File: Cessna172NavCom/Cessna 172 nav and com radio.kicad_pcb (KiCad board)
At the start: 2 copper layers, 180 x 98 mm, 95 parts, among them J1 EN11-HSM1BF20, J2 USB_B_Micro, J3 EN11-HSM1BF20, J4 EN11-HSM1BF20, J5 EN11-HSM1BF20, J6 EN11-HSM1BF20, J7 EN11-HSM1BF20, J8 Conn_02x20_Odd_Even, SW1 SW_Push, SW2 SW_Push, SW3 SW_Push, SW4 SW_Push, SW5 SW_Push, SW6 SW_Push, U1 MAX7219 COM standby, U10 3651A, U11 MAX7219 COM standby, U12 3651A, U13 MAX7219 COM standby, U14 3651A, U15 MAX7219 COM standby, U16 3651A, U2 3651A, U3 MAX7219 COM standby, U4 3651A, U5 MAX7219 COM standby, U6 3651A, U7 MAX7219 COM standby, U8 3651A, U9 MAX7219 COM standby

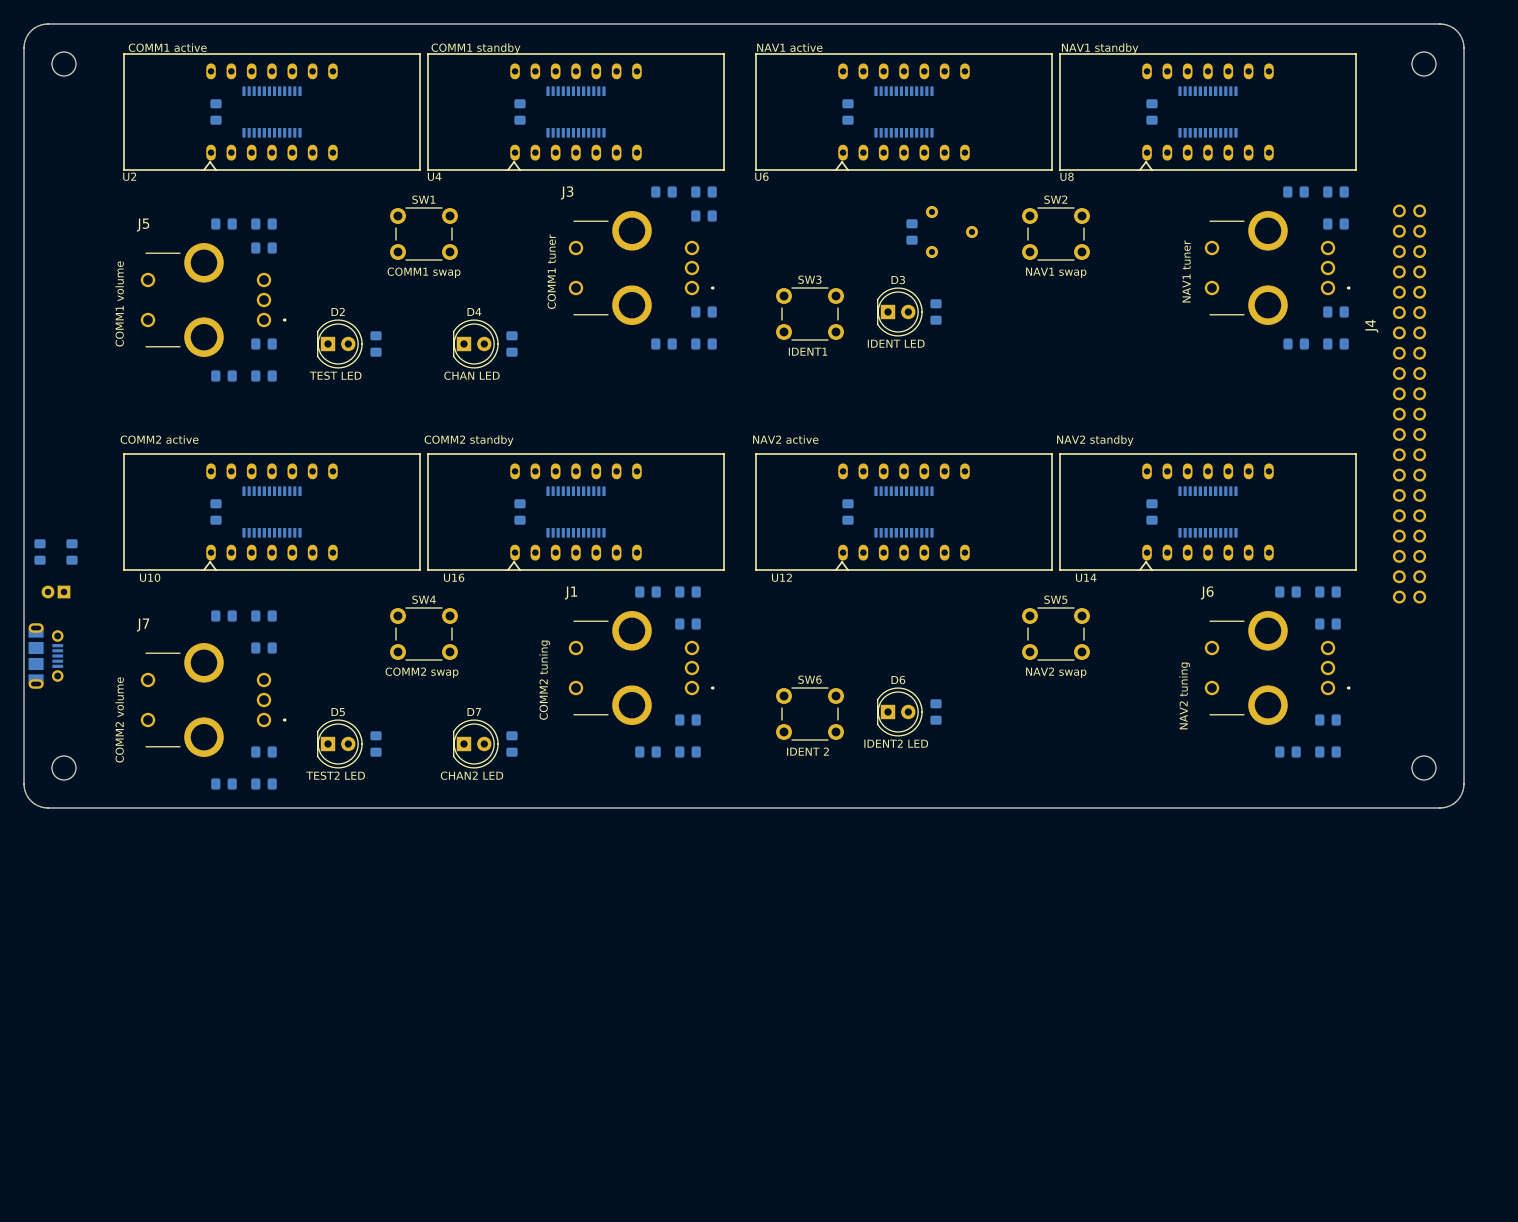
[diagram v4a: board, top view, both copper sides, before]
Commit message: Position changes for routing
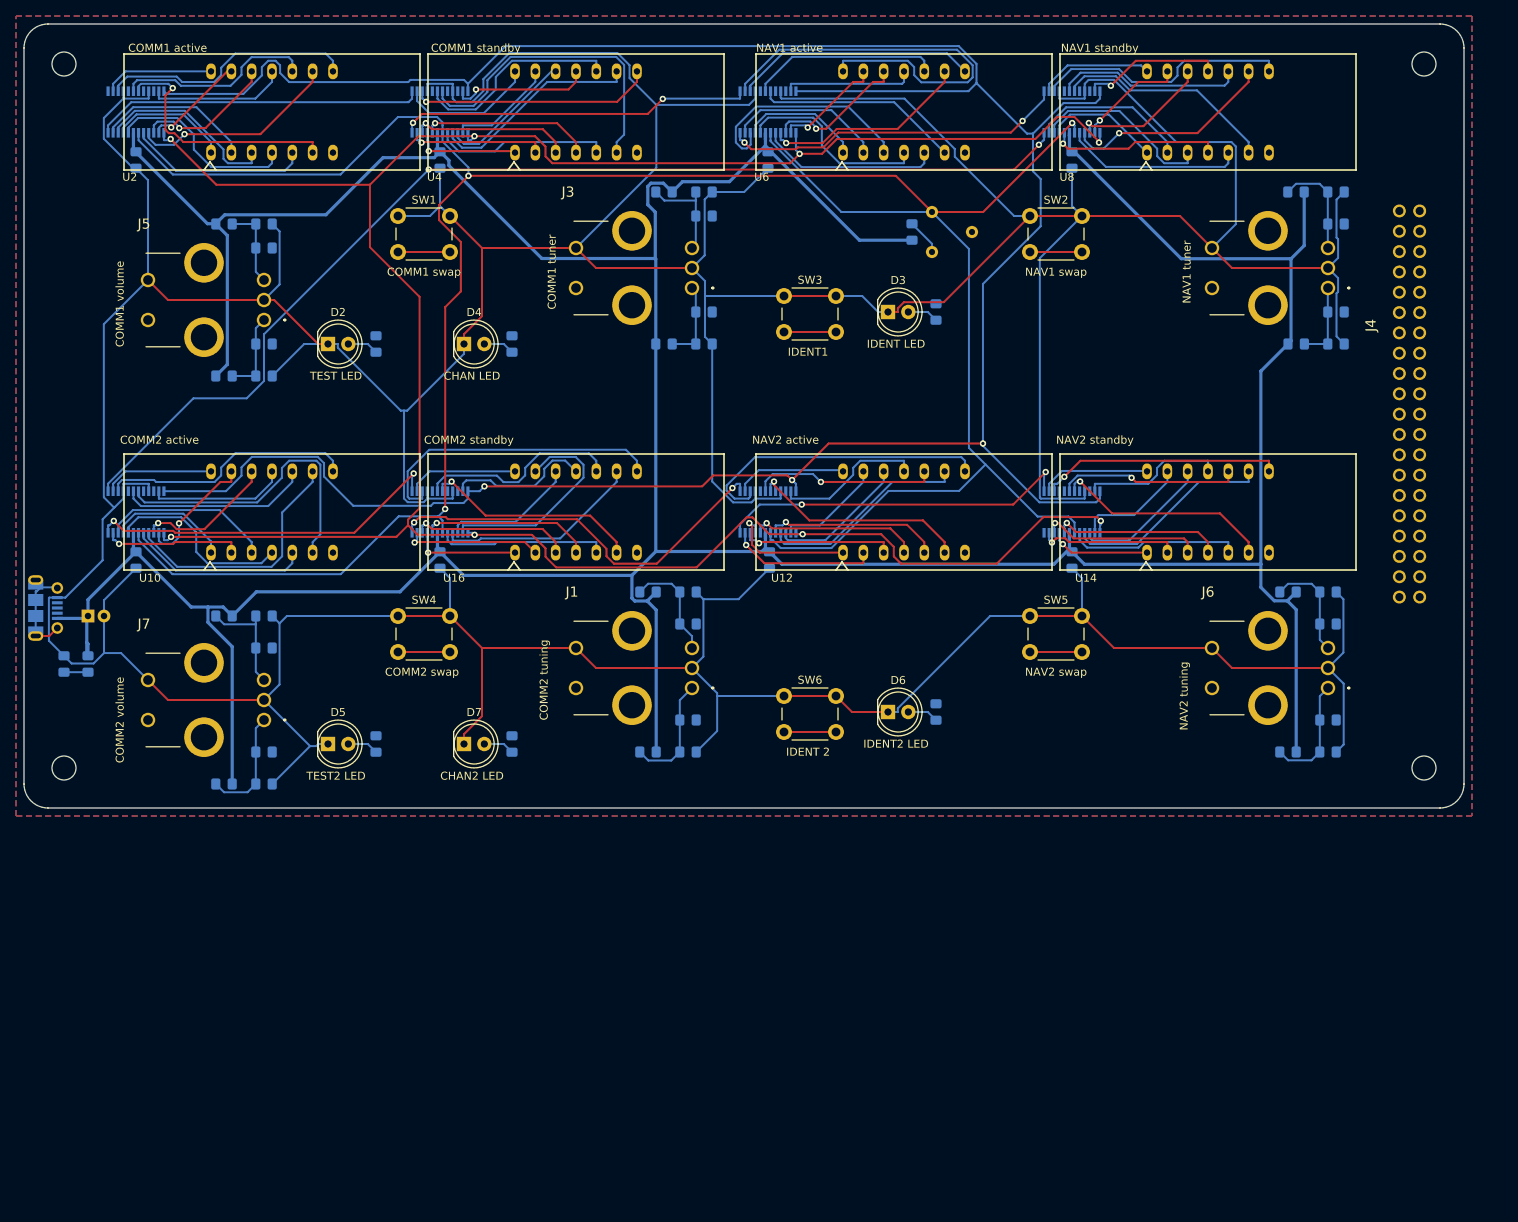
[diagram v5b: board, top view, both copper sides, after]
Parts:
- moved U1 17.0 mm to (44.0, 41.0)
- moved U11 17.0 mm to (123.0, 91.0)
- moved U13 17.0 mm to (161.0, 91.0)
- moved U15 17.0 mm to (82.0, 91.0)
- moved U3 17.0 mm to (82.0, 41.0)
- moved U5 17.0 mm to (123.0, 41.0)
- moved U7 17.0 mm to (161.0, 41.0)
- moved U9 17.0 mm to (44.0, 91.0)
- moved D1 14.3 mm to (35.0, 110.0), turned to 270 degrees
- moved R2 14.1 mm to (38.0, 110.0)
- moved C12 11.7 mm to (44.0, 97.0)
- moved C13 11.7 mm to (82.0, 97.0)
- moved C15 11.7 mm to (161.0, 97.0)
- moved C2 11.7 mm to (44.0, 47.0), turned to 270 degrees
- moved C3 11.7 mm to (82.0, 47.0), turned to 270 degrees
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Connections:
- U10 pad 7: (no net) -> Net-(U10-Pad7)
- U12 pad 7: (no net) -> Net-(U12-Pad7)
- U14 pad 7: (no net) -> Net-(U14-Pad7)
- U16 pad 7: (no net) -> Net-(U16-Pad7)
- U2 pad 7: (no net) -> Net-(U2-Pad7)
- U4 pad 7: (no net) -> Net-(U4-Pad7)
- U6 pad 7: (no net) -> Net-(U6-Pad7)
- U8 pad 7: (no net) -> Net-(U8-Pad7)
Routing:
- net GND: track 0.00 -> 904.7 mm
- net +5V: track 0.00 -> 539.0 mm
- net ISET: track 0.00 -> 334.3 mm, vias 0 -> 3
- net LOAD: track 0.00 -> 331.2 mm, vias 0 -> 3
- net CLK: track 0.00 -> 313.8 mm, vias 0 -> 8
- net /sheet5F68A9C2/DIN: track 0.00 -> 140.1 mm, vias 0 -> 2
- net /sheet5F613960/DIG_0: track 0.00 -> 53.0 mm
- net /sheet5F68A9C3/DIN: track 0.00 -> 50.4 mm, vias 0 -> 2
- net /sheet5F68A9C5/DIN: track 0.00 -> 45.3 mm, vias 0 -> 2
- net /sheet5F68A9C4/DIN: track 0.00 -> 44.5 mm, vias 0 -> 2
- net /sheet5F613960/DIN: track 0.00 -> 44.4 mm, vias 0 -> 2
- net /sheet5F613961/DIN: track 0.00 -> 43.0 mm, vias 0 -> 2
- net /sheet5F611637/DIN: track 0.00 -> 41.2 mm
- net /sheet5F611637/DIG_3: track 0.00 -> 39.2 mm
- net /sheet5F68A9C2/DIG_3: track 0.00 -> 38.2 mm
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- added copper zone on B.Cu, net GND
- added copper zone on F.Cu, net GND
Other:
- rule trace_min: 0.2 -> 0.15
- rule via_min_size: 0.4 -> 0.3

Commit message: Move things around to try and help router
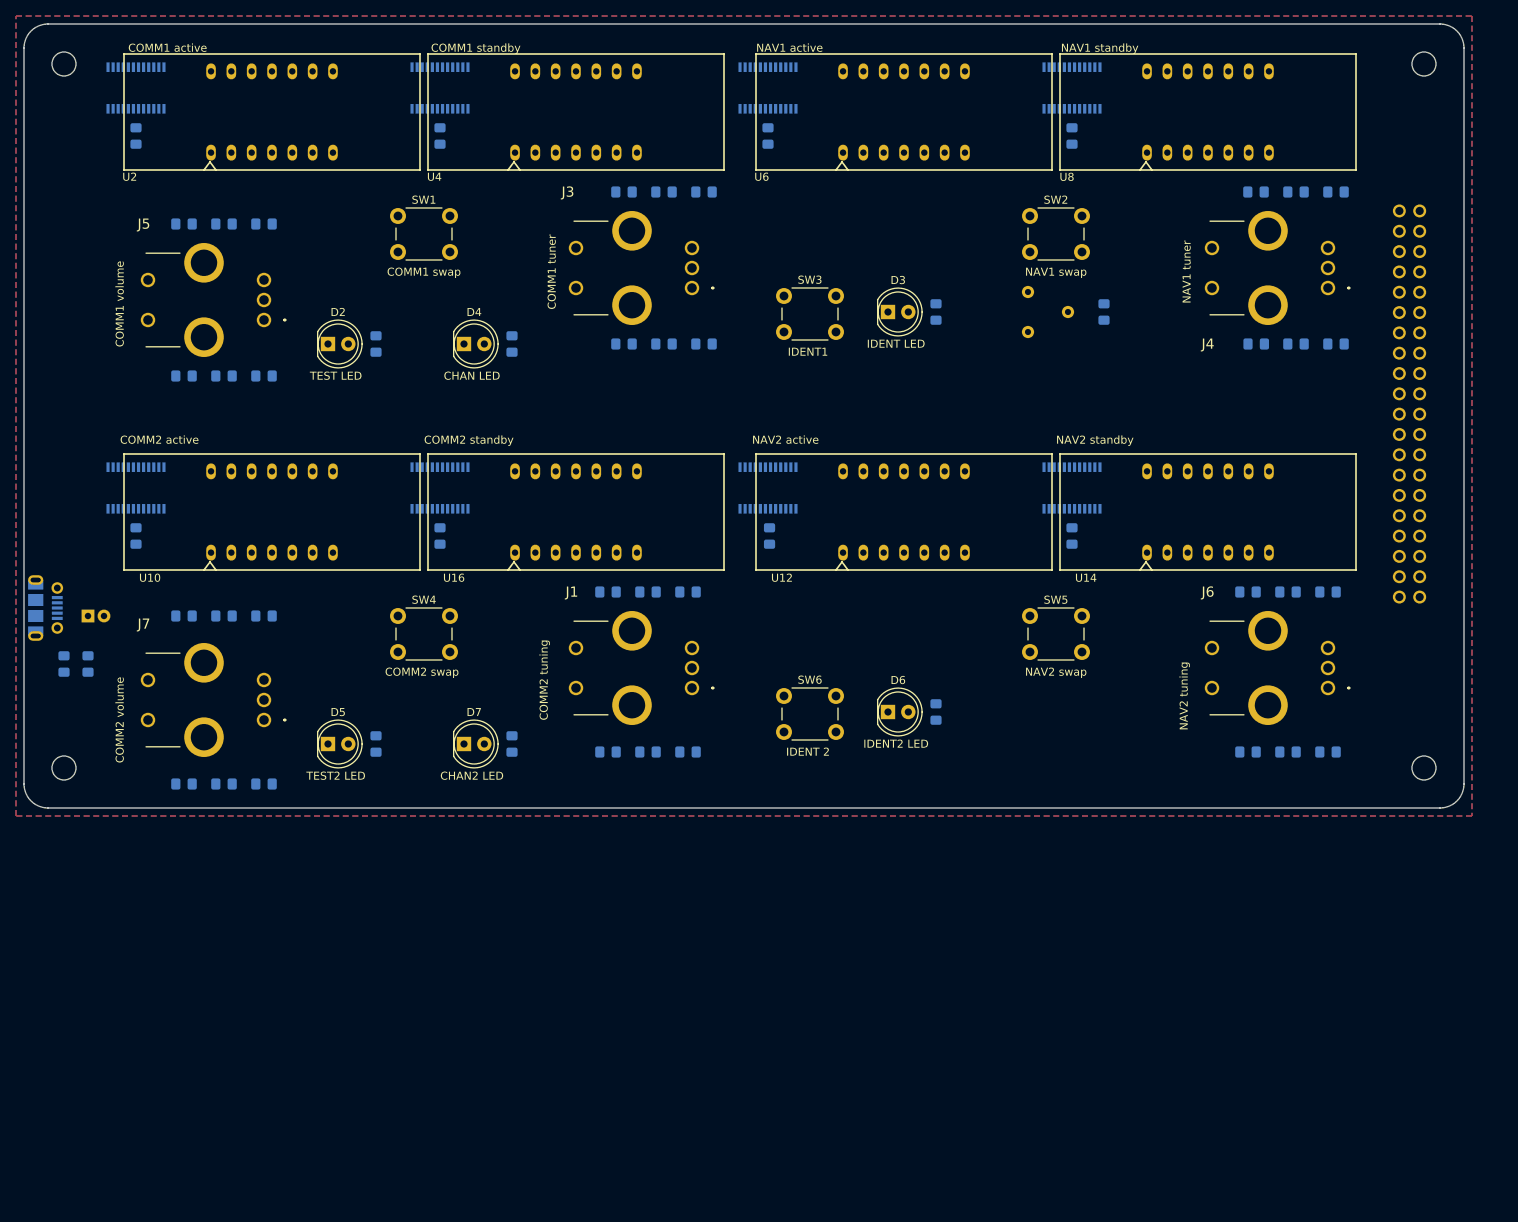
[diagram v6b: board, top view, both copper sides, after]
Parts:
- moved R1 26.0 mm to (165.0, 66.0), turned to 270 degrees
- moved RV1 15.6 mm to (158.0, 66.0)
- moved C10 5.00 mm to (55.0, 74.0)
- moved C11 5.00 mm to (55.0, 55.0)
- moved C16 5.00 mm to (108.0, 121.0)
- moved C17 5.00 mm to (108.0, 101.0)
- moved C18 5.00 mm to (188.0, 121.0)
- moved C19 5.00 mm to (188.0, 101.0)
- moved C20 5.00 mm to (55.0, 125.0)
- moved C21 5.00 mm to (55.0, 104.0)
- moved C6 5.00 mm to (110.0, 70.0)
- moved C7 5.00 mm to (110.0, 51.0)
- moved C8 5.00 mm to (189.0, 70.0)
- moved C9 5.00 mm to (189.0, 51.0)
- moved R10 5.00 mm to (184.0, 51.0)
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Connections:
- J8 pad 27: TEST1_SW -> Net-(J8-Pad27)
- J8 pad 28: TEST2_SW -> Net-(J8-Pad28)
- J8 pad 29: TEST1_LED -> Net-(J8-Pad29)
- J8 pad 30: TEST2_LED -> Net-(J8-Pad30)
- J8 pad 31: IDENT1_SW -> TEST1_SW
- J8 pad 32: IDENT2_SW -> TEST2_SW
- J8 pad 33: IDENT1_LED -> TEST1_LED
- J8 pad 34: IDENT2_LED -> TEST2_LED
- J8 pad 35: CHAN1_LED -> IDENT1_SW
- J8 pad 36: CHAN2_LED -> IDENT2_SW
- J8 pad 37: Net-(J8-Pad37) -> IDENT1_LED
- J8 pad 38: Net-(J8-Pad38) -> IDENT2_LED
- J8 pad 39: Net-(J8-Pad39) -> CHAN1_LED
- J8 pad 40: Net-(J8-Pad40) -> CHAN2_LED
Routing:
- net GND: track 904.7 -> 0.00 mm
- net +5V: track 539.0 -> 0.00 mm
- net ISET: track 334.3 -> 0.00 mm, vias 3 -> 0
- net LOAD: track 331.2 -> 0.00 mm, vias 3 -> 0
- net CLK: track 313.8 -> 0.00 mm, vias 8 -> 0
- net /sheet5F68A9C2/DIN: track 140.1 -> 0.00 mm, vias 2 -> 0
- net /sheet5F613960/DIG_0: track 53.0 -> 0.00 mm
- net /sheet5F68A9C3/DIN: track 50.4 -> 0.00 mm, vias 2 -> 0
- net /sheet5F68A9C5/DIN: track 45.3 -> 0.00 mm, vias 2 -> 0
- net /sheet5F68A9C4/DIN: track 44.5 -> 0.00 mm, vias 2 -> 0
- net /sheet5F613960/DIN: track 44.4 -> 0.00 mm, vias 2 -> 0
- net /sheet5F613961/DIN: track 43.0 -> 0.00 mm, vias 2 -> 0
- net /sheet5F611637/DIN: track 41.2 -> 0.00 mm
- net /sheet5F611637/DIG_3: track 39.2 -> 0.00 mm
- net /sheet5F68A9C2/DIG_3: track 38.2 -> 0.00 mm
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
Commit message: Fix courtyard overlap for routing
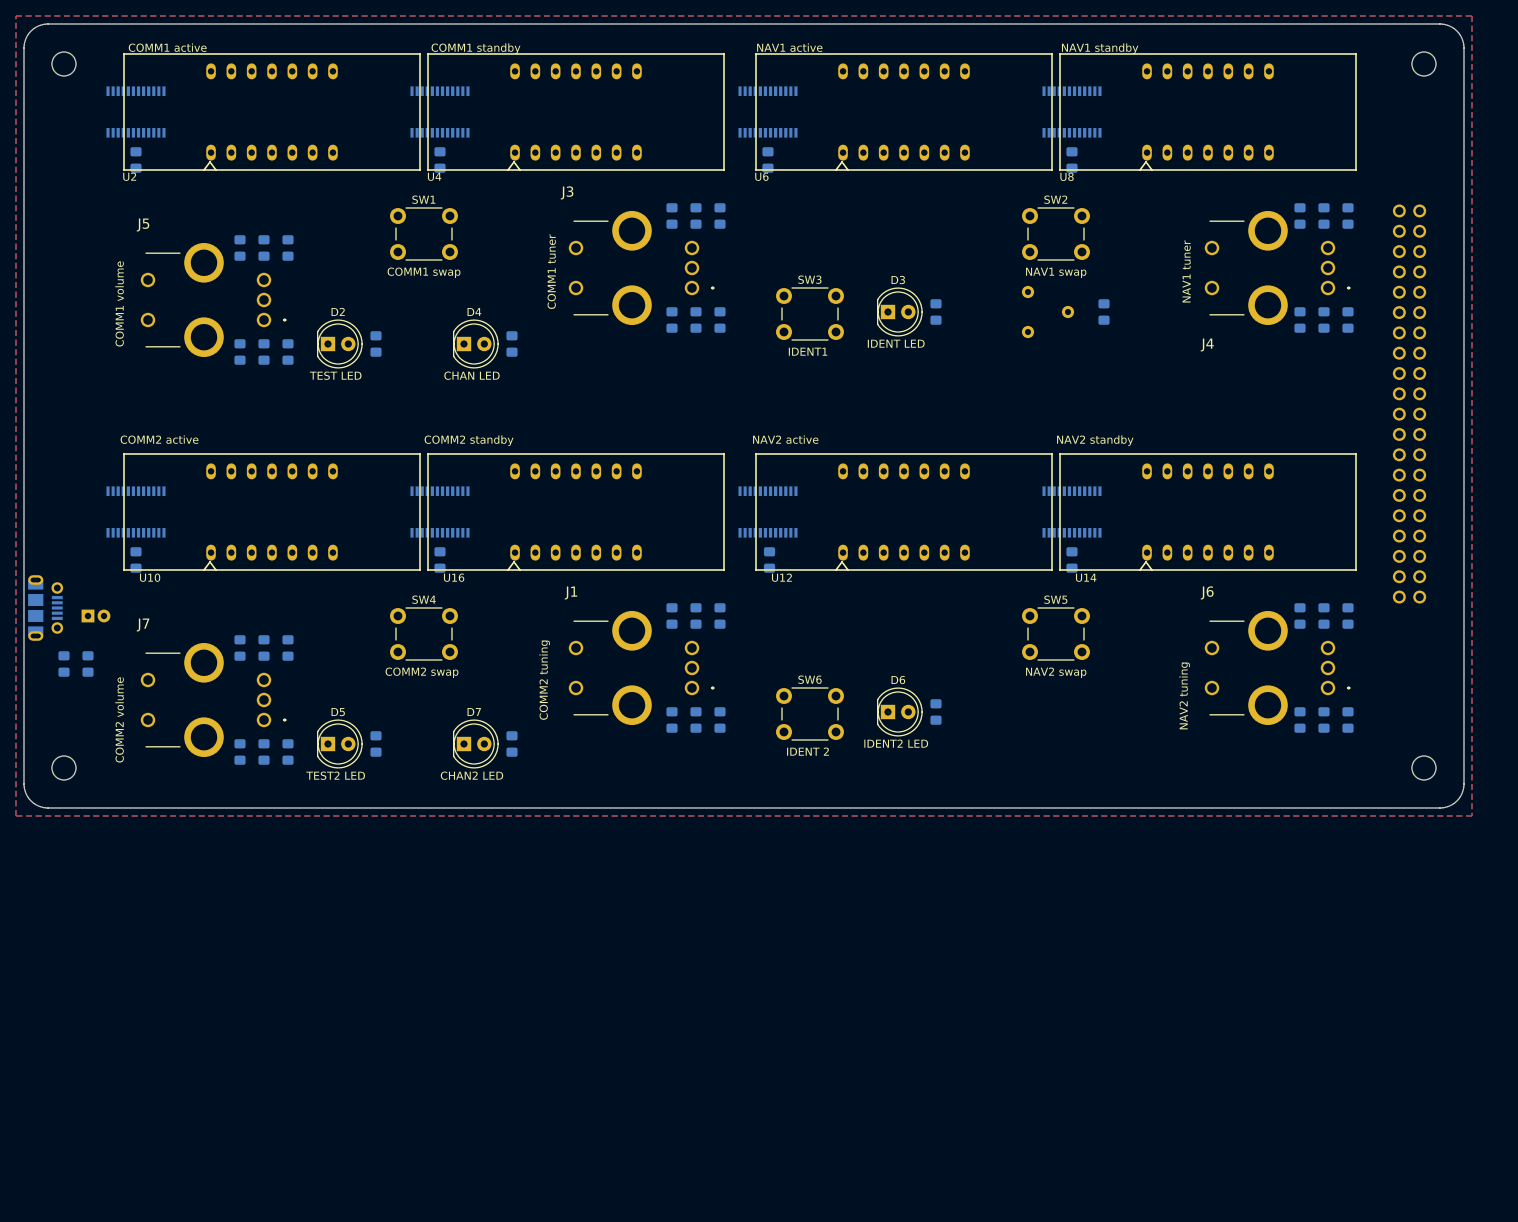
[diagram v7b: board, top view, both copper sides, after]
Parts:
- moved R14 13.3 mm to (63.0, 58.0), turned to 270 degrees
- moved R21 8.94 mm to (111.0, 117.0), turned to 90 degrees
- moved R22 8.54 mm to (111.0, 104.0), turned to 90 degrees
- moved R29 8.06 mm to (57.0, 121.0), turned to 90 degrees
- moved R30 8.06 mm to (57.0, 108.0), turned to 90 degrees
- moved R25 7.63 mm to (189.5, 117.0), turned to 90 degrees
- moved R13 7.62 mm to (57.0, 71.0), turned to 90 degrees
- moved C16 7.21 mm to (114.0, 117.0), turned to 90 degrees
- moved R26 7.16 mm to (189.5, 104.0), turned to 90 degrees
- moved C17 6.71 mm to (114.0, 104.0), turned to 90 degrees
- moved R5 6.71 mm to (111.0, 67.0), turned to 90 degrees
- moved R6 6.71 mm to (111.0, 54.0), turned to 90 degrees
- moved C20 6.40 mm to (60.0, 121.0), turned to 90 degrees
- moved C21 6.40 mm to (60.0, 108.0), turned to 90 degrees
- moved R10 6.26 mm to (189.5, 54.0), turned to 90 degrees
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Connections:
- C12 pad 1: Net-(C12-Pad1) -> +5V
- C12 pad 2: Net-(C12-Pad2) -> GND
- C13 pad 1: Net-(C12-Pad1) -> +5V
- C13 pad 2: Net-(C12-Pad2) -> GND
- C14 pad 1: Net-(C12-Pad1) -> +5V
- C14 pad 2: Net-(C12-Pad2) -> GND
- C15 pad 1: Net-(C12-Pad1) -> +5V
- C15 pad 2: Net-(C12-Pad2) -> GND
- C2 pad 1: Net-(C12-Pad1) -> +5V
- C2 pad 2: Net-(C12-Pad2) -> GND
- C3 pad 1: Net-(C12-Pad1) -> +5V
- C3 pad 2: Net-(C12-Pad2) -> GND
- C4 pad 1: Net-(C12-Pad1) -> +5V
- C4 pad 2: Net-(C12-Pad2) -> GND
- C5 pad 1: Net-(C12-Pad1) -> +5V
- C5 pad 2: Net-(C12-Pad2) -> GND
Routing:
- added copper zone on B.Cu, net (none)
- added copper zone on F.Cu, net (none)
- removed copper zone on B.Cu, net GND
- removed copper zone on F.Cu, net GND
